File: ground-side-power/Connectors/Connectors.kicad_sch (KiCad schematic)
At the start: 11 parts, among them J15 To Router, J16 To RLCS, J17 To DAQ Laptop, J18 Conn_01x02_Female, J19 Conn_01x02_Female, J20 To Ethernet, J21 To 5V M12, J22 To DAQ, J23 Extra M12, J24 Extra M12, J25 Extra M12

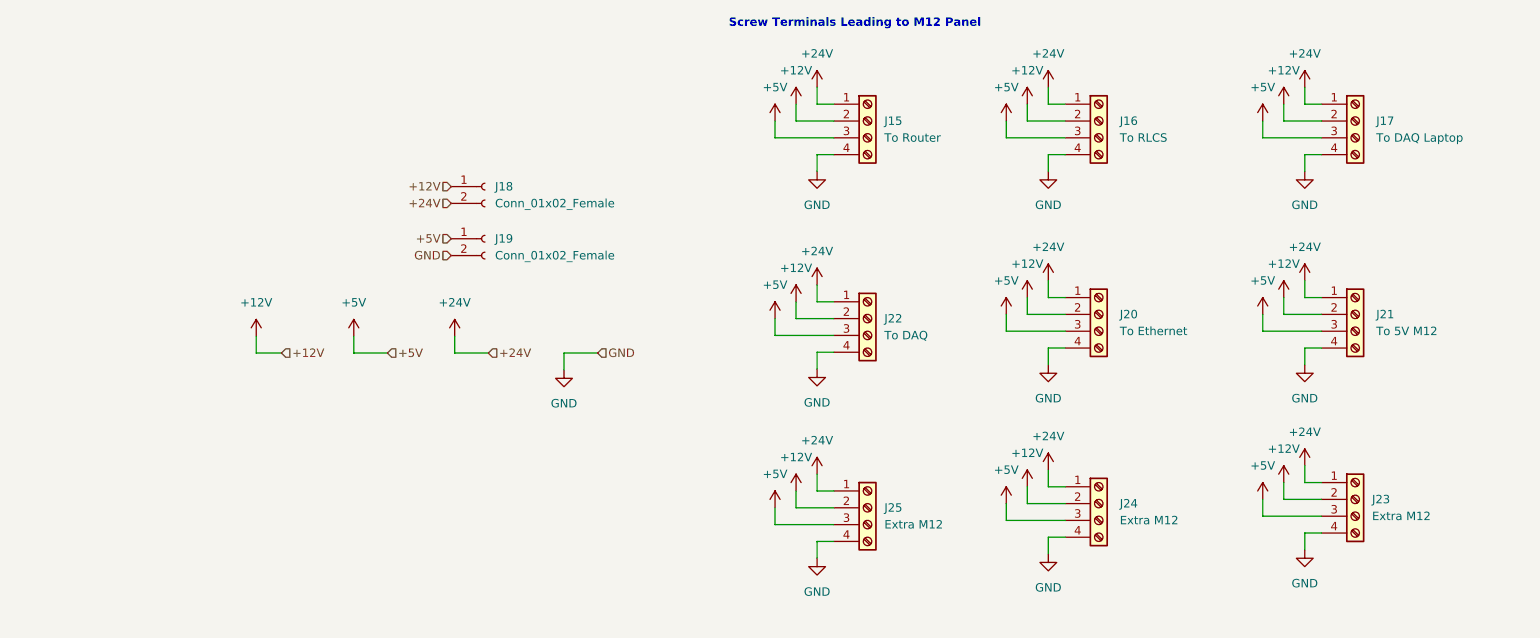
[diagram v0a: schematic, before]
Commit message: Added Fan Headers + Thermistor
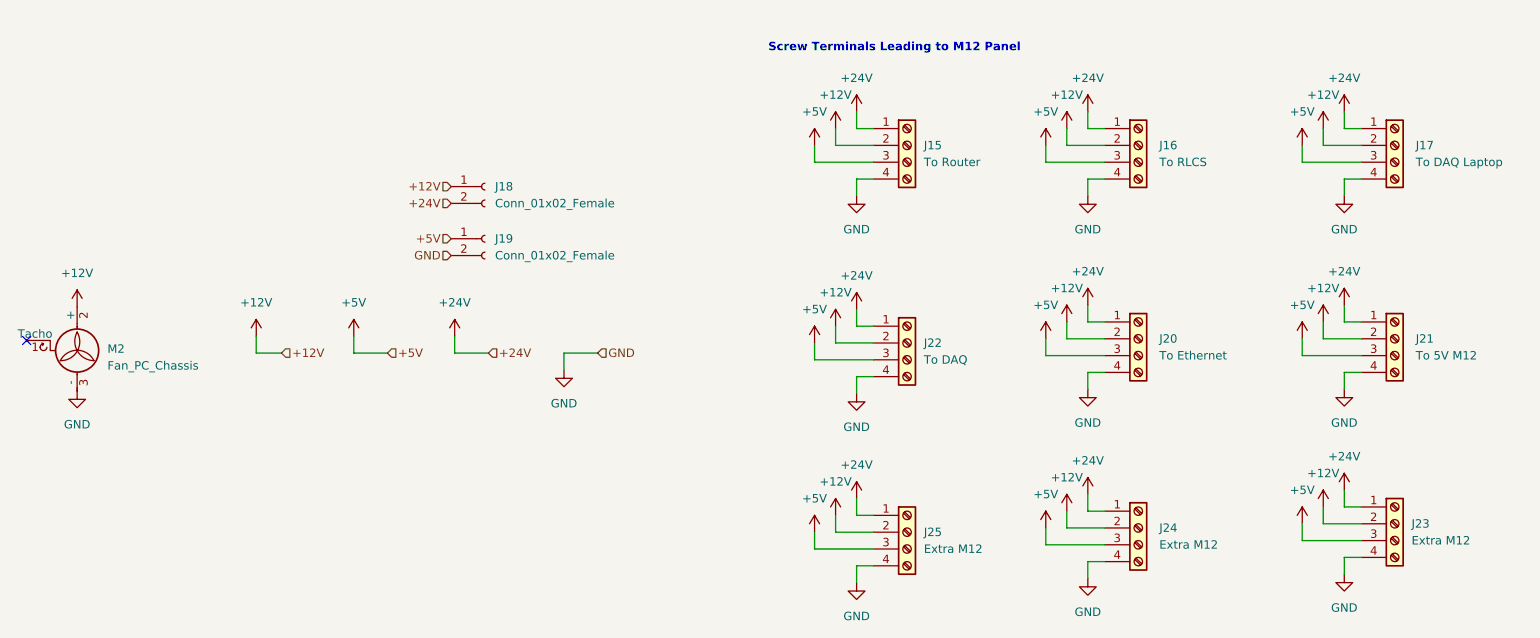
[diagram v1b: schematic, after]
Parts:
- added M2: Fan_PC_Chassis, Connector:FanPinHeader_1x03_P2.54mm_Vertical, symbol Motor:Fan_PC_Chassis
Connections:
- net +12V: now also M2.2 (+)
- net GND: now also M2.3 (-)
- no-connect marks 0 -> 1

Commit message: PCB Layout First Draft
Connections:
- net +12V: now also J19.2 (Pin_2); no longer J18.1 (Pin_1)
- net GND: now also J18.1 (Pin_1); no longer J19.2 (Pin_2)
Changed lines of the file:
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@@
     (effects (font (size 1.27 1.27)) (justify left))
   )
-  (hierarchical_label "+12V" (shape input) (at 83.185 83.185 180)
+  (hierarchical_label "+12V" (shape input) (at 83.312 93.98 180)
     (effects (font (size 1.27 1.27)) (justify right))
   )
@@
     (effects (font (size 1.27 1.27)) (justify left))
   )
-  (hierarchical_label "GND" (shape input) (at 83.185 93.599 180)
-    (effects (font (size 1.27 1.27)) (justify right))
-  )
-  (hierarchical_label "+5V" (shape input) (at 83.185 91.059 180)
-    (effects (font (size 1.27 1.27)) (justify right))
-  )
-  (hierarchical_label "+24V" (shape input) (at 83.185 85.725 180)
+  (hierarchical_label "GND" (shape input) (at 83.312 83.566 180)
+    (effects (font (size 1.27 1.27)) (justify right))
+  )
+  (hierarchical_label "+5V" (shape input) (at 83.312 91.44 180)
+    (effects (font (size 1.27 1.27)) (justify right))
+  )
+  (hierarchical_label "+24V" (shape input) (at 83.312 86.106 180)
     (effects (font (size 1.27 1.27)) (justify right))
   )
@@
     (pin "1")
   )
-  (symbol (lib_id "Connector:Conn_01x02_Female") (at 88.265 83.185 0) (unit 1)
-    (in_bom yes) (on_board yes) (fields_autoplaced)
-    (property "Reference" "J18" (id 0) (at 89.789 83.1849 0)
-      (effects (font (size 1.27 1.27)) (justify left))
-    )
-    (property "Value" "Conn_01x02_Female" (id 1) (at 89.789 85.7249 0)
-      (effects (font (size 1.27 1.27)) (justify left))
-    )
-    (property "Footprint" "GSP:OSTTA020161" (id 2) (at 88.265 83.185 0)
-      (effects (font (size 1.27 1.27)) hide)
-    )
-    (property "Datasheet" "~" (id 3) (at 88.265 83.185 0)
+  (symbol (lib_id "Connector:Conn_01x02_Female") (at 88.392 83.566 0) (unit 1)
+    (in_bom yes) (on_board yes) (fields_autoplaced)
+    (property "Reference" "J18" (id 0) (at 89.916 83.5659 0)
+      (effects (font (size 1.27 1.27)) (justify left))
+    )
+    (property "Value" "Conn_01x02_Female" (id 1) (at 89.916 86.1059 0)
+      (effects (font (size 1.27 1.27)) (justify left))
+    )
+    (property "Footprint" "GSP:OSTTA020161" (id 2) (at 88.392 83.566 0)
+      (effects (font (size 1.27 1.27)) hide)
+    )
+    (property "Datasheet" "~" (id 3) (at 88.392 83.566 0)
       (effects (font (size 1.27 1.27)) hide)
     )
@@
     (pin "1")
   )
-  (symbol (lib_id "Connector:Conn_01x02_Female") (at 88.265 91.059 0) (unit 1)
-    (in_bom yes) (on_board yes) (fields_autoplaced)
-    (property "Reference" "J19" (id 0) (at 89.789 91.0589 0)
-      (effects (font (size 1.27 1.27)) (justify left))
-    )
-    (property "Value" "Conn_01x02_Female" (id 1) (at 89.789 93.5989 0)
-      (effects (font (size 1.27 1.27)) (justify left))
-    )
-    (property "Footprint" "GSP:OSTTA020161" (id 2) (at 88.265 91.059 0)
-      (effects (font (size 1.27 1.27)) hide)
-    )
-    (property "Datasheet" "~" (id 3) (at 88.265 91.059 0)
-      (effects (font (size 1.27 1.27)) hide)
-    )
+  (symbol (lib_id "Connector:Conn_01x02_Female") (at 88.392 91.44 0) (unit 1)
+    (in_bom yes) (on_board yes) (fields_autoplaced)
+    (property "Reference" "J19" (id 0) (at 89.916 91.4399 0)
+      (effects (font (size 1.27 1.27)) (justify left))
+    )
+    (property "Value" "Conn_01x02_Female" (id 1) (at 89.916 93.9799 0)
+      (effects (font (size 1.27 1.27)) (justify left))
+    )
+    (property "Footprint" "GSP:OSTTA020161" (id 2) (at 88.392 91.44 0)
+      (effects (font (size 1.27 1.27)) hide)
+    )
+    (property "Datasheet" "~" (id 3) (at 88.392 91.44 0)
+      (effects (font (size 1.27 1.27)) hide)
+    )

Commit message: Address Input and Converter Comments
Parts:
- J15, J16, J17, J20, J21, J22, J23, J24, J25: footprint GSP:EB21A-04-D -> GSP:CUI_TB008A-508-04BE
- J18, J19: footprint GSP:OSTTA020161 -> GSP:1935310
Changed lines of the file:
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@@
       (effects (font (size 1.27 1.27)) (justify left))
     )
-    (property "Footprint" "GSP:OSTTA020161" (id 2) (at 88.392 83.566 0)
+    (property "Footprint" "GSP:1935310" (id 2) (at 88.392 83.566 0)
       (effects (font (size 1.27 1.27)) hide)
     )
@@
       (effects (font (size 1.27 1.27)) (justify left))
     )
-    (property "Footprint" "GSP:EB21A-04-D" (id 2) (at 152.019 135.382 0)
+    (property "Footprint" "GSP:CUI_TB008A-508-04BE" (id 2) (at 152.019 135.382 0)
       (effects (font (size 1.27 1.27)) hide)
     )
@@
       (effects (font (size 1.27 1.27)) (justify left))
     )
-    (property "Footprint" "GSP:EB21A-04-D" (id 2) (at 225.679 76.962 0)
+    (property "Footprint" "GSP:CUI_TB008A-508-04BE" (id 2) (at 225.679 76.962 0)
       (effects (font (size 1.27 1.27)) hide)
     )
@@
       (effects (font (size 1.27 1.27)) (justify left))
     )
-    (property "Footprint" "GSP:EB21A-04-D" (id 2) (at 186.944 134.747 0)
+    (property "Footprint" "GSP:CUI_TB008A-508-04BE" (id 2) (at 186.944 134.747 0)
       (effects (font (size 1.27 1.27)) hide)
     )
@@
       (effects (font (size 1.27 1.27)) (justify left))
     )
-    (property "Footprint" "GSP:EB21A-04-D" (id 2) (at 152.019 76.962 0)
+    (property "Footprint" "GSP:CUI_TB008A-508-04BE" (id 2) (at 152.019 76.962 0)
       (effects (font (size 1.27 1.27)) hide)
     )
@@
       (effects (font (size 1.27 1.27)) (justify left))
     )
-    (property "Footprint" "GSP:OSTTA020161" (id 2) (at 88.392 91.44 0)
+    (property "Footprint" "GSP:1935310" (id 2) (at 88.392 91.44 0)
       (effects (font (size 1.27 1.27)) hide)
     )
@@
       (effects (font (size 1.27 1.27)) (justify left))
     )
-    (property "Footprint" "GSP:EB21A-04-D" (id 2) (at 225.679 134.112 0)
+    (property "Footprint" "GSP:CUI_TB008A-508-04BE" (id 2) (at 225.679 134.112 0)
       (effects (font (size 1.27 1.27)) hide)
     )
@@
       (effects (font (size 1.27 1.27)) (justify left))
     )
-    (property "Footprint" "GSP:EB21A-04-D" (id 2) (at 186.944 76.962 0)
+    (property "Footprint" "GSP:CUI_TB008A-508-04BE" (id 2) (at 186.944 76.962 0)
       (effects (font (size 1.27 1.27)) hide)
     )
@@
       (effects (font (size 1.27 1.27)) (justify left))
     )
-    (property "Footprint" "GSP:EB21A-04-D" (id 2) (at 152.019 106.807 0)
+    (property "Footprint" "GSP:CUI_TB008A-508-04BE" (id 2) (at 152.019 106.807 0)
       (effects (font (size 1.27 1.27)) hide)
     )
@@
       (effects (font (size 1.27 1.27)) (justify left))
     )
-    (property "Footprint" "GSP:EB21A-04-D" (id 2) (at 225.679 106.172 0)
+    (property "Footprint" "GSP:CUI_TB008A-508-04BE" (id 2) (at 225.679 106.172 0)
       (effects (font (size 1.27 1.27)) hide)
     )
@@
       (effects (font (size 1.27 1.27)) (justify left))
     )
-    (property "Footprint" "GSP:EB21A-04-D" (id 2) (at 186.944 106.172 0)
-      (effects (font (size 1.27 1.27)) hide)
-    )
+    (property "Footprint" "GSP:CUI_TB008A-508-04BE" (id 2) (at 186.944 106.172 0)
+      (effects (font (size 1.27 1.27)) hide)
+    )

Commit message: Resolved Final Issues
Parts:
- removed J19: Conn_01x02_Female, GSP:1935310, symbol Connector:Conn_01x02_Female
- added J19: Conn_01x02_Female, GSP:1935323, symbol Connector:Conn_01x03_Female
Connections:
- net +12V: now also J18.1 (Pin_1)
- net +24V: now also J19.1 (Pin_1); no longer J18.2 (Pin_2)
- net +5V: now also J19.3 (Pin_3)
- net GND: now also J18.2 (Pin_2), J19.2 (Pin_2); no longer J18.1 (Pin_1)

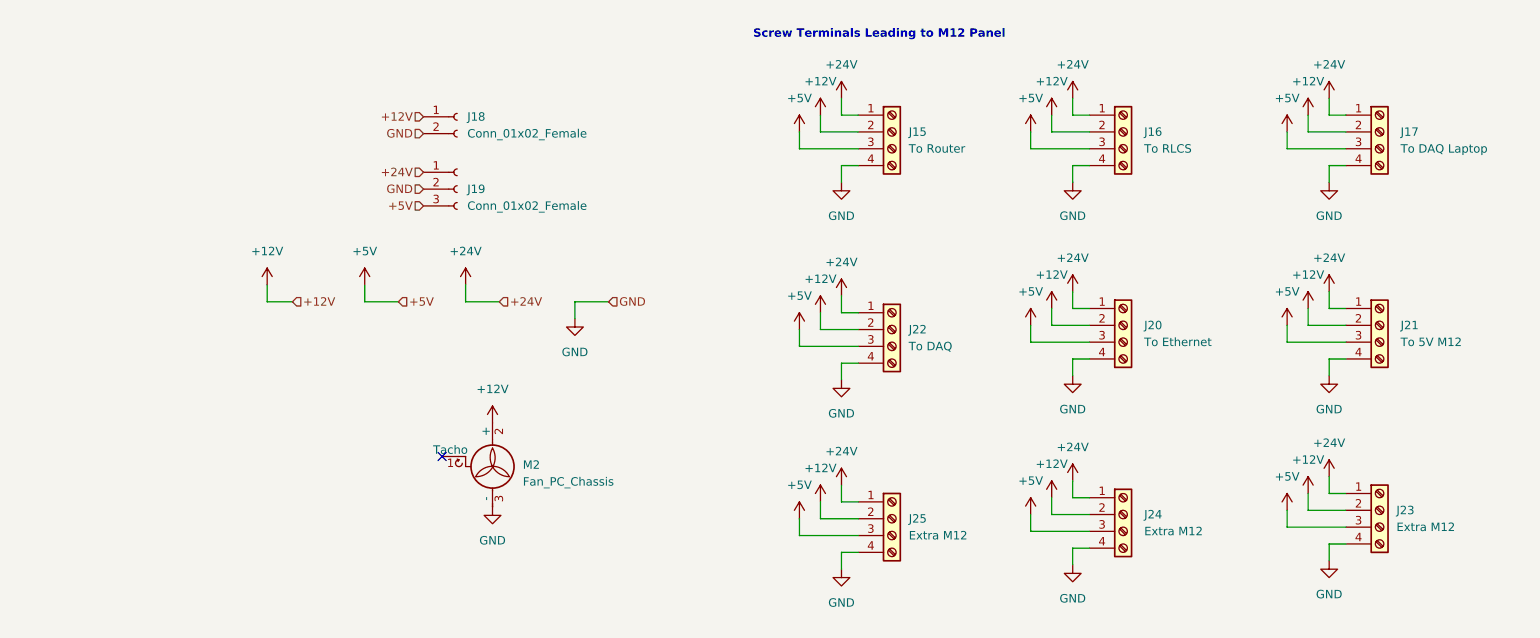
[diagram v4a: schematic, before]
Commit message: Updated Fuses
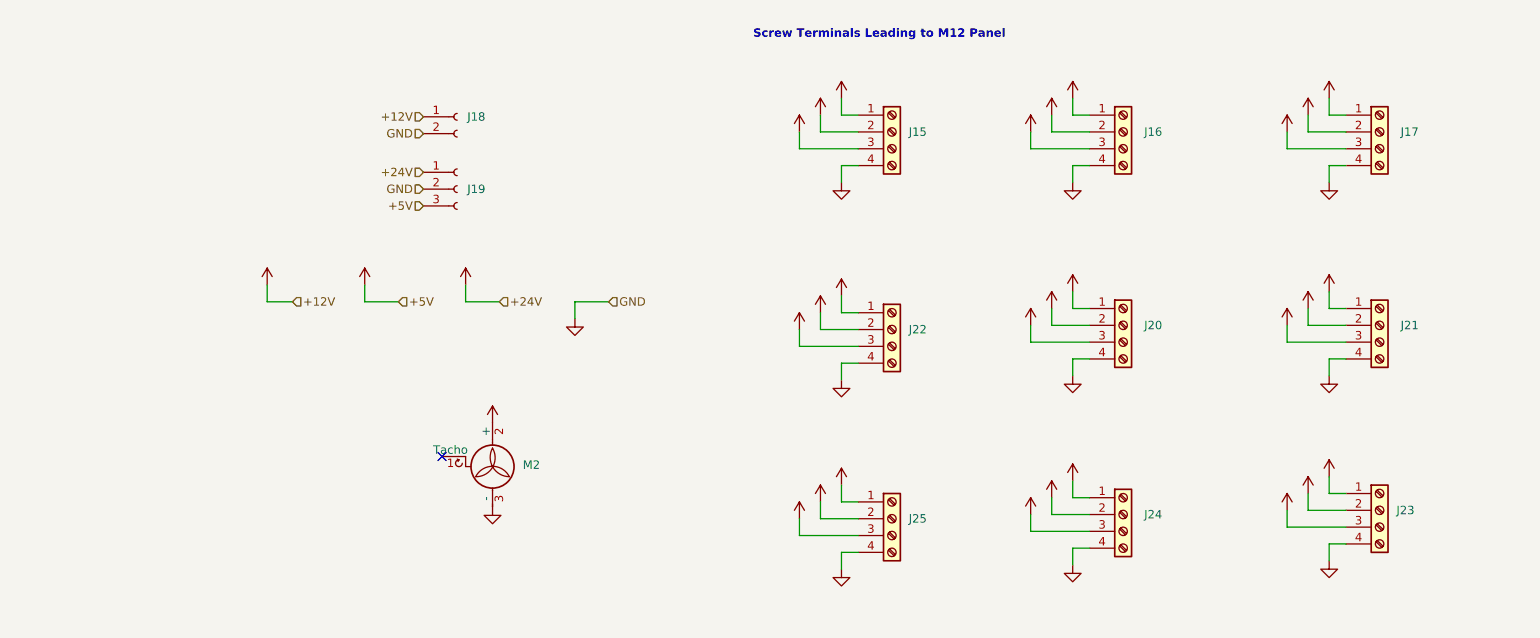
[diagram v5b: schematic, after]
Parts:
- J15: value To Router -> (none); footprint GSP:CUI_TB008A-508-04BE -> (none)
- J16: value To RLCS -> (none); footprint GSP:CUI_TB008A-508-04BE -> (none)
- J17: value To DAQ Laptop -> (none); footprint GSP:CUI_TB008A-508-04BE -> (none)
- J18: value Conn_01x02_Female -> (none); footprint GSP:1935310 -> (none)
- J19: value Conn_01x02_Female -> (none); footprint GSP:1935323 -> (none)
- J20: value To Ethernet -> (none); footprint GSP:CUI_TB008A-508-04BE -> (none)
- J21: value To 5V M12 -> (none); footprint GSP:CUI_TB008A-508-04BE -> (none)
- J22: value To DAQ -> (none); footprint GSP:CUI_TB008A-508-04BE -> (none)
- J23, J24, J25: value Extra M12 -> (none); footprint GSP:CUI_TB008A-508-04BE -> (none)
- M2: value Fan_PC_Chassis -> (none); footprint Connector:FanPinHeader_1x03_P2.54mm_Vertical -> (none)
